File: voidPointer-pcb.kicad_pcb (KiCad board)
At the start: 2 copper layers, 304.9 x 122.8 mm, 154 parts, among them SW1 KEYSW, SW10 KEYSW, SW11 KEYSW, SW12 KEYSW, SW13 KEYSW, SW14 KEYSW, SW15 KEYSW, SW16 KEYSW, SW17 KEYSW, SW18 KEYSW, SW19 KEYSW, SW2 KEYSW, SW20 KEYSW, SW21 KEYSW, SW22 KEYSW, SW23 KEYSW, SW24 KEYSW, SW25 KEYSW, SW26 KEYSW, SW27 KEYSW, SW28 KEYSW, SW29 KEYSW, SW3 KEYSW, SW30 KEYSW, SW31 KEYSW, SW32 KEYSW, SW33 KEYSW, SW34 KEYSW, SW35 KEYSW, SW36 KEYSW, SW37 KEYSW, SW38 KEYSW, SW39 KEYSW, SW4 KEYSW, SW40 KEYSW, SW41 KEYSW, SW42 KEYSW, SW43 KEYSW, SW44 KEYSW, SW45 KEYSW, SW46 KEYSW, SW47 KEYSW, SW48 KEYSW, SW49 KEYSW, SW5 KEYSW, SW50 KEYSW, SW51 KEYSW, SW52 KEYSW, SW53 KEYSW, SW54 KEYSW, SW55 KEYSW, SW56 KEYSW, SW57 KEYSW, SW58 KEYSW, SW59 KEYSW, SW6 KEYSW, SW60 KEYSW, SW61 KEYSW, SW62 KEYSW, SW63 KEYSW, SW64 KEYSW, SW65 KEYSW, SW66 KEYSW, SW67 KEYSW, SW68 KEYSW, SW7 KEYSW, SW79 SW_SPST, SW8 KEYSW, SW9 KEYSW, U1 SuperMini nRF52840

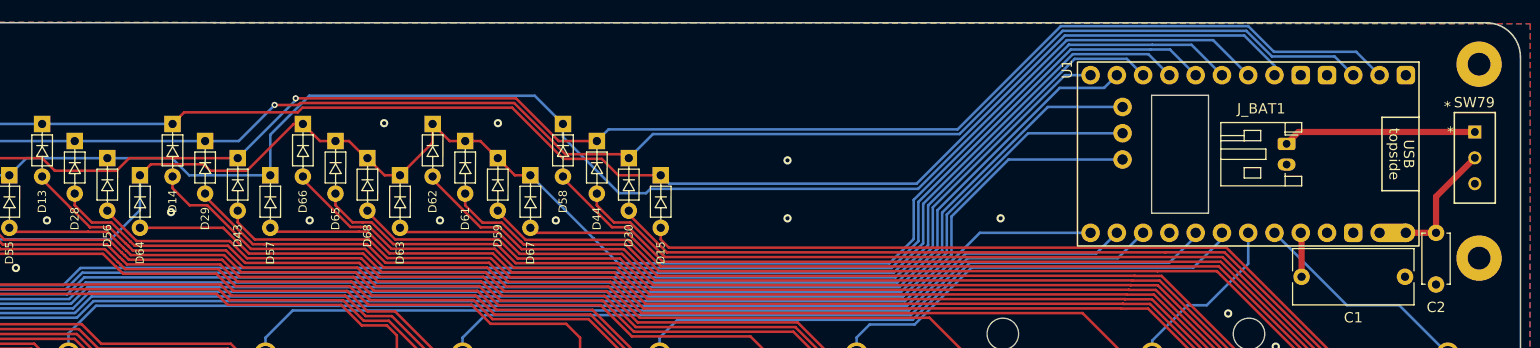
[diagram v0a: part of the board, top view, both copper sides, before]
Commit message: Fixing small issues on the project and updating readme
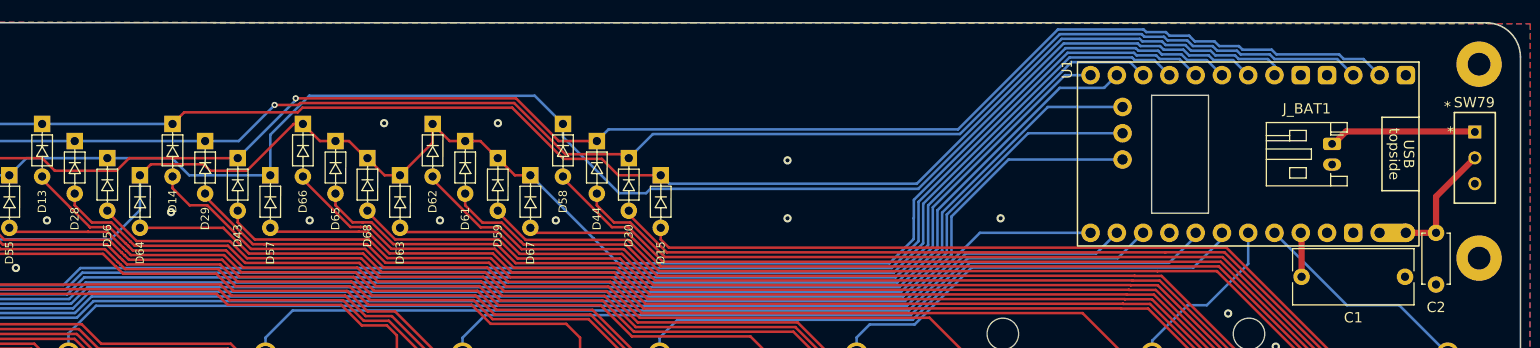
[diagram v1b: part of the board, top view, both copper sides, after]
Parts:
- moved J_BAT1 4.40 mm to (340.4, 69.4)
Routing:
- net V_BAT: track 18.7 -> 14.3 mm
